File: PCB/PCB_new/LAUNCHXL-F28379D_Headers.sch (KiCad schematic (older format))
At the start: 5 parts, among them U1 TI_CONN

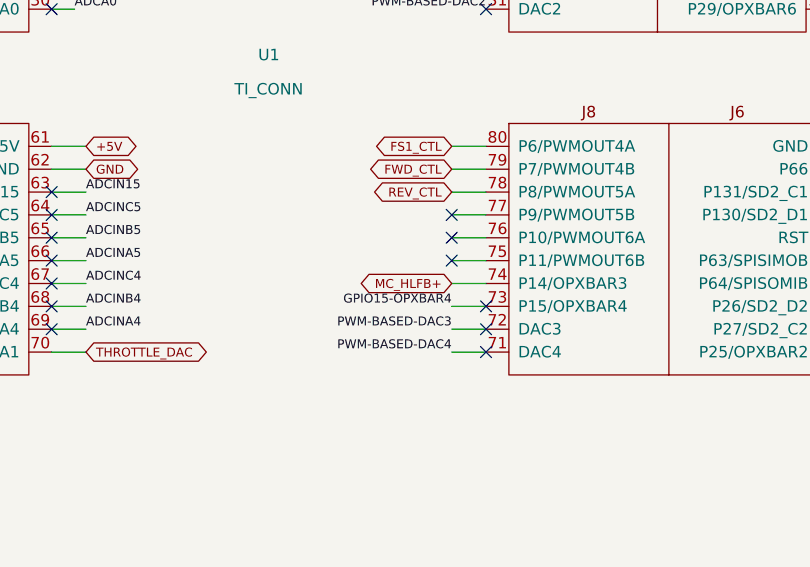
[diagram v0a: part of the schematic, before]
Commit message: removed signals to HLFB+ for steering motor
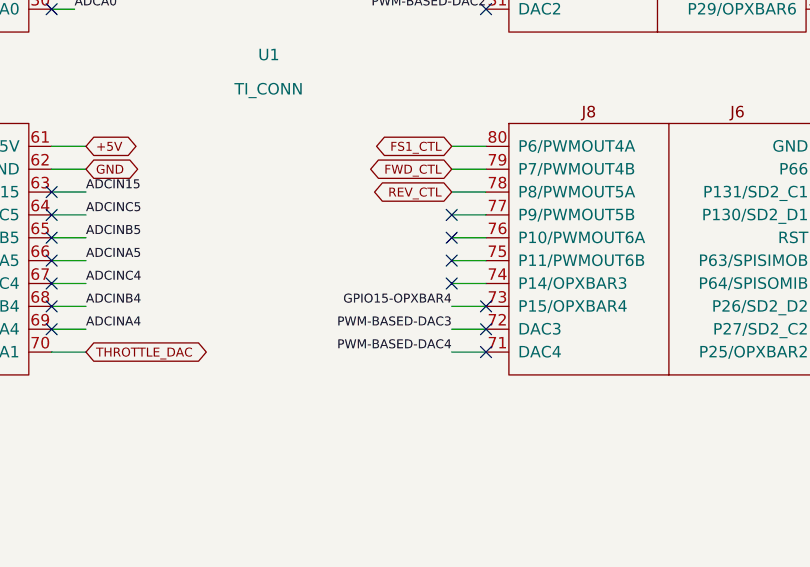
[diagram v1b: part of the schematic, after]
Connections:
- net MC_HLFB+: no longer names the net of U1.74 (P14/OPXBAR3)
- no-connect marks 58 -> 59
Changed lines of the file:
@@
 Text Label 8150 4150 2    39   ~ 0
 GPIO15-OPXBAR4
-Text GLabel 8150 4050 0    39   BiDi ~ 0
-MC_HLFB+
 Text GLabel 8150 3650 0    39   BiDi ~ 0
 REV_CTL
@@
 Wire Wire Line
 	10000 3850 9850 3850
-$Comp
-L PCB_2020:TI_CONN U1
-U 1 1 5E10AD09
-P 7300 3100
-F 0 "U1" H 7350 3150 50  0000 C CNN
-F 1 "TI_CONN" H 7350 3000 50  0000 C CNN
-F 2 "Drivetrain_control:TI_Footprint" H 7300 3100 50  0001 C CNN
-F 3 "https://www.digikey.com/product-detail/en/te-connectivity-amp-connectors/826629-2/A105107-ND/1130753?utm_adgroup=Connectors%20&%20Interconnects&utm_source=google&utm_medium=cpc&utm_campaign=Dynamic%20Search&utm_term=&utm_content=Connectors%20&%20Interconnects&gclid=CjwKCAiA3uDwBRBFEiwA1VsajFpRq2OjG4RmtuGXWOX3NBMJTcv1glxE23z1SpbbgeTgjMK5AdF2YRoC3S4QAvD_BwE" H 7300 3150 50  0001 C CNN
-	1    7300 3100
-	1    0    0    -1
-$EndComp
 Wire Wire Line
 	5100 4350 4950 4350
@@
 NoConn ~ 4950 4250
 NoConn ~ 4950 4350
+$Comp
+L PCB_2020:TI_CONN U1
+U 1 1 5E10AD09
+P 7300 3100
+F 0 "U1" H 7350 3150 50  0000 C CNN
+F 1 "TI_CONN" H 7350 3000 50  0000 C CNN
+F 2 "Drivetrain_control:TI_Footprint" H 7300 3100 50  0001 C CNN
+F 3 "https://www.digikey.com/product-detail/en/te-connectivity-amp-connectors/826629-2/A105107-ND/1130753?utm_adgroup=Connectors%20&%20Interconnects&utm_source=google&utm_medium=cpc&utm_campaign=Dynamic%20Search&utm_term=&utm_content=Connectors%20&%20Interconnects&gclid=CjwKCAiA3uDwBRBFEiwA1VsajFpRq2OjG4RmtuGXWOX3NBMJTcv1glxE23z1SpbbgeTgjMK5AdF2YRoC3S4QAvD_BwE" H 7300 3150 50  0001 C CNN
+	1    7300 3100
+	1    0    0    -1
+$EndComp
+NoConn ~ 8150 4050
 $EndSCHEMATC

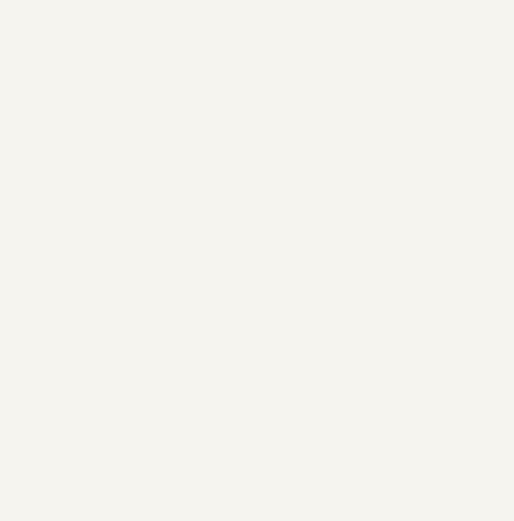
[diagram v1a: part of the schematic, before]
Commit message: added mounting holes
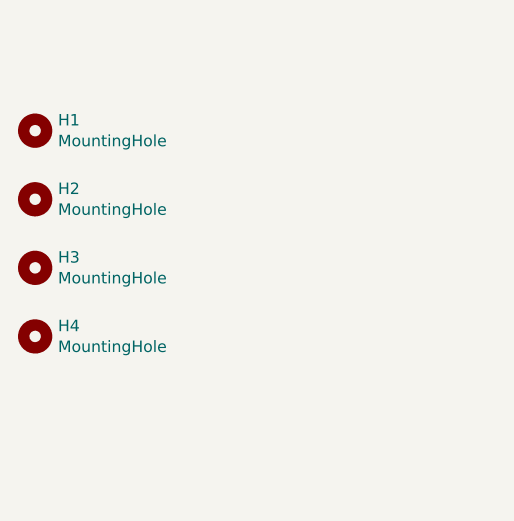
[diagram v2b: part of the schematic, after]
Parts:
- added H1, H2, H3, H4: MountingHole, MountingHole:MountingHole_3.5mm, symbol Mechanical:MountingHole
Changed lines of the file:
@@
 $EndComp
 NoConn ~ 8150 4050
+$Comp
+L Mechanical:MountingHole H1
+U 1 1 5E1FD379
+P 1150 2200
+F 0 "H1" H 1250 2246 50  0000 L CNN
+F 1 "MountingHole" H 1250 2155 50  0000 L CNN
+F 2 "MountingHole:MountingHole_3.5mm" H 1150 2200 50  0001 C CNN
+F 3 "~" H 1150 2200 50  0001 C CNN
+	1    1150 2200
+	1    0    0    -1
+$EndComp
+$Comp
+L Mechanical:MountingHole H2
+U 1 1 5E1FDA5D
+P 1150 2500
+F 0 "H2" H 1250 2546 50  0000 L CNN
+F 1 "MountingHole" H 1250 2455 50  0000 L CNN
+F 2 "MountingHole:MountingHole_3.5mm" H 1150 2500 50  0001 C CNN
+F 3 "~" H 1150 2500 50  0001 C CNN
+	1    1150 2500
+	1    0    0    -1
+$EndComp
+$Comp
+L Mechanical:MountingHole H3
+U 1 1 5E1FDD41
+P 1150 2800
+F 0 "H3" H 1250 2846 50  0000 L CNN
+F 1 "MountingHole" H 1250 2755 50  0000 L CNN
+F 2 "MountingHole:MountingHole_3.5mm" H 1150 2800 50  0001 C CNN
+F 3 "~" H 1150 2800 50  0001 C CNN
+	1    1150 2800
+	1    0    0    -1
+$EndComp
+$Comp
+L Mechanical:MountingHole H4
+U 1 1 5E1FDF2B
+P 1150 3100
+F 0 "H4" H 1250 3146 50  0000 L CNN
+F 1 "MountingHole" H 1250 3055 50  0000 L CNN
+F 2 "MountingHole:MountingHole_3.5mm" H 1150 3100 50  0001 C CNN
+F 3 "~" H 1150 3100 50  0001 C CNN
+	1    1150 3100
+	1    0    0    -1
+$EndComp
 $EndSCHEMATC

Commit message: revised mounting holes to 2.5mm
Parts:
- H1, H2, H3, H4: footprint MountingHole:MountingHole_3.5mm -> MountingHole:MountingHole_2.5mm
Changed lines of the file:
@@
 F 0 "H1" H 1250 2246 50  0000 L CNN
 F 1 "MountingHole" H 1250 2155 50  0000 L CNN
-F 2 "MountingHole:MountingHole_3.5mm" H 1150 2200 50  0001 C CNN
+F 2 "MountingHole:MountingHole_2.5mm" H 1150 2200 50  0001 C CNN
 F 3 "~" H 1150 2200 50  0001 C CNN
 	1    1150 2200
@@
 $Comp
 L Mechanical:MountingHole H2
-U 1 1 5E1FDA5D
+U 1 1 5E27C5D4
 P 1150 2500
 F 0 "H2" H 1250 2546 50  0000 L CNN
 F 1 "MountingHole" H 1250 2455 50  0000 L CNN
-F 2 "MountingHole:MountingHole_3.5mm" H 1150 2500 50  0001 C CNN
+F 2 "MountingHole:MountingHole_2.5mm" H 1150 2500 50  0001 C CNN
 F 3 "~" H 1150 2500 50  0001 C CNN
 	1    1150 2500
@@
 $Comp
 L Mechanical:MountingHole H3
-U 1 1 5E1FDD41
+U 1 1 5E27C92D
 P 1150 2800
 F 0 "H3" H 1250 2846 50  0000 L CNN
 F 1 "MountingHole" H 1250 2755 50  0000 L CNN
-F 2 "MountingHole:MountingHole_3.5mm" H 1150 2800 50  0001 C CNN
+F 2 "MountingHole:MountingHole_2.5mm" H 1150 2800 50  0001 C CNN
 F 3 "~" H 1150 2800 50  0001 C CNN
 	1    1150 2800
@@
 $Comp
 L Mechanical:MountingHole H4
-U 1 1 5E1FDF2B
+U 1 1 5E27CB44
 P 1150 3100
 F 0 "H4" H 1250 3146 50  0000 L CNN
 F 1 "MountingHole" H 1250 3055 50  0000 L CNN
-F 2 "MountingHole:MountingHole_3.5mm" H 1150 3100 50  0001 C CNN
+F 2 "MountingHole:MountingHole_2.5mm" H 1150 3100 50  0001 C CNN
 F 3 "~" H 1150 3100 50  0001 C CNN
 	1    1150 3100

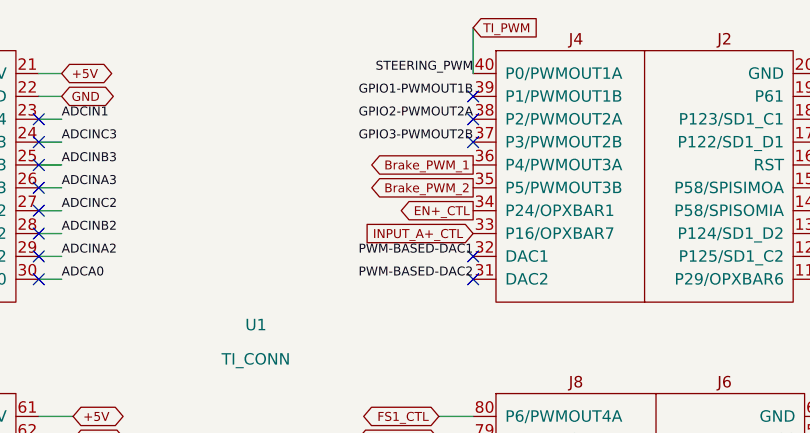
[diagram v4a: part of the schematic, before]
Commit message: moved braking PWM to PWM2A and PWM3A
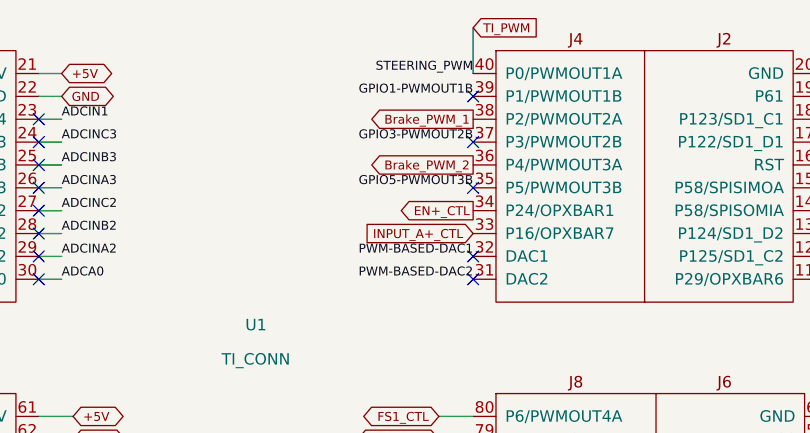
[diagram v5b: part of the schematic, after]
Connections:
- net GPIO2-PWMOUT2A is gone; now on net Brake_PWM_1: U1.38 (P2/PWMOUT2A)
- net Brake_PWM_1: no longer U1.36 (P4/PWMOUT3A)
- net Brake_PWM_2: now also U1.36 (P4/PWMOUT3A); no longer U1.35 (P5/PWMOUT3B)
- new net GPIO5-PWMOUT3B: U1.35 (P5/PWMOUT3B)
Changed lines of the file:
@@
 Text Label 10000 4350 0    39   ~ 0
 GPIO25-OPXBAR2
-Text Label 8300 2150 2    39   ~ 0
-GPIO2-PWMOUT2A
 Text GLabel 8300 2650 0    39   Input ~ 0
 INPUT_A+_CTL
@@
 Text Label 8300 2750 2    39   ~ 0
 PWM-BASED-DAC1
-Text Label 8300 2250 2    39   ~ 0
-GPIO3-PWMOUT2B
 Text Label 8300 2050 2    39   ~ 0
 GPIO1-PWMOUT1B
@@
 NoConn ~ 6400 4250
 NoConn ~ 8300 2050
-NoConn ~ 8300 2150
 NoConn ~ 8300 2250
 NoConn ~ 8300 2750
@@
 Wire Wire Line
 	3300 6500 3800 6500
-Text GLabel 8300 2450 0    39   Output ~ 0
+Text GLabel 8300 2350 0    39   Output ~ 0
 Brake_PWM_2
-Text GLabel 8300 2350 0    39   Output ~ 0
+Text GLabel 8300 2150 0    39   Output ~ 0
 Brake_PWM_1
 Wire Wire Line
@@
 	1    0    0    -1
 $EndComp
+Text Label 8300 2250 2    39   ~ 0
+GPIO3-PWMOUT2B
+NoConn ~ 8300 2450
+Text Label 8300 2450 2    39   ~ 0
+GPIO5-PWMOUT3B
 $EndSCHEMATC

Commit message: increased size of screw holes from 2.5mm to 2.7mm
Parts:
- H1, H2, H3, H4: footprint MountingHole:MountingHole_2.5mm -> MountingHole:MountingHole_2.7mm
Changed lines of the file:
@@
 F 0 "H1" H 1250 2246 50  0000 L CNN
 F 1 "MountingHole" H 1250 2155 50  0000 L CNN
-F 2 "MountingHole:MountingHole_2.5mm" H 1150 2200 50  0001 C CNN
+F 2 "MountingHole:MountingHole_2.7mm" H 1150 2200 50  0001 C CNN
 F 3 "https://www.adafruit.com/product/3299" H 1150 2200 50  0001 C CNN
 	1    1150 2200
@@
 F 0 "H2" H 1250 2546 50  0000 L CNN
 F 1 "MountingHole" H 1250 2455 50  0000 L CNN
-F 2 "MountingHole:MountingHole_2.5mm" H 1150 2500 50  0001 C CNN
+F 2 "MountingHole:MountingHole_2.7mm" H 1150 2500 50  0001 C CNN
 F 3 "https://www.adafruit.com/product/3299" H 1150 2500 50  0001 C CNN
 	1    1150 2500
@@
 F 0 "H3" H 1250 2846 50  0000 L CNN
 F 1 "MountingHole" H 1250 2755 50  0000 L CNN
-F 2 "MountingHole:MountingHole_2.5mm" H 1150 2800 50  0001 C CNN
+F 2 "MountingHole:MountingHole_2.7mm" H 1150 2800 50  0001 C CNN
 F 3 "https://www.adafruit.com/product/3299" H 1150 2800 50  0001 C CNN
 	1    1150 2800
@@
 F 0 "H4" H 1250 3146 50  0000 L CNN
 F 1 "MountingHole" H 1250 3055 50  0000 L CNN
-F 2 "MountingHole:MountingHole_2.5mm" H 1150 3100 50  0001 C CNN
+F 2 "MountingHole:MountingHole_2.7mm" H 1150 3100 50  0001 C CNN
 F 3 "https://www.adafruit.com/product/3299" H 1150 3100 50  0001 C CNN
 	1    1150 3100

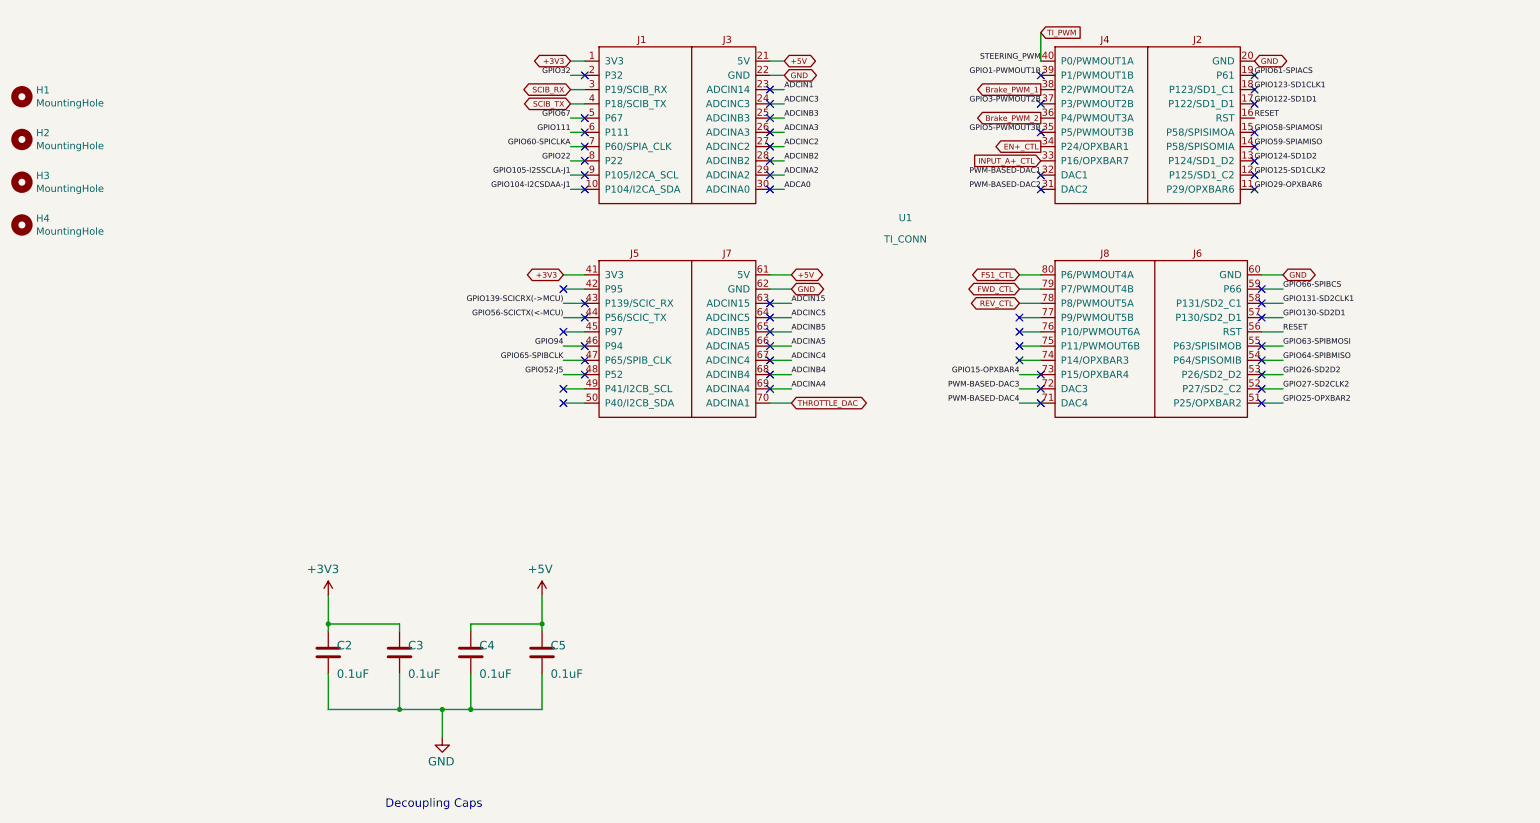
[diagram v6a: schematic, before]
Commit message: added arduino due .lib and footprint files
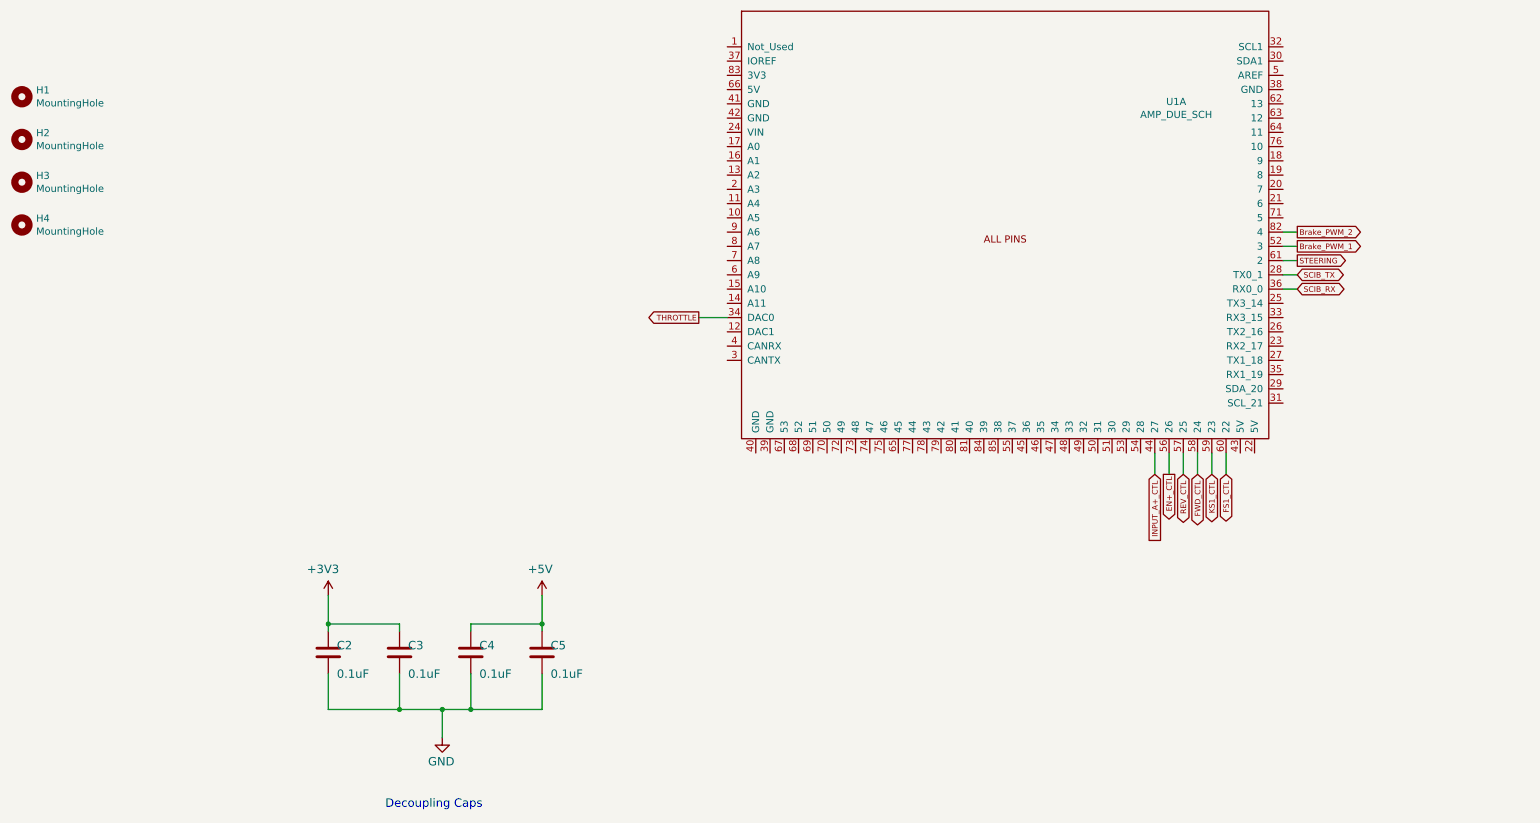
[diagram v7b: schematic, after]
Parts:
- removed U1: TI_CONN, Drivetrain_control:TI_Footprint, symbol PCB_2020:TI_CONN
- added U1: AMP_DUE_SCH, DUE Footprint:Arduino DUE, symbol PCB_2020:AMP_DUE_SCH
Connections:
- net Brake_PWM_1: now also U1.52 (3)
- net Brake_PWM_2: now also U1.82 (4)
- net EN+_CTL: now also U1.56 (26)
- net FS1_CTL: now also U1.60 (22)
- net FWD_CTL: now also U1.58 (24)
- net INPUT_A+_CTL: now also U1.44 (27)
- net REV_CTL: now also U1.57 (25)
- net SCIB_RX: now also U1.36 (RX0_0)
- net SCIB_TX: now also U1.28 (TX0_1)
- new net KS1_CTL: U1.59 (23)
- new net STEERING: U1.61 (2)
- new net THROTTLE: U1.34 (DAC0)
- no-connect marks 59 -> 0
